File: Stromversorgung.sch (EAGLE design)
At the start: 16 parts, among them J1 DCJ0202, U1 TSR 2-2450, U2 TSR 1-2433, U3 TSR 2-2450, X1 Ein/Aus, X2 MAC64L

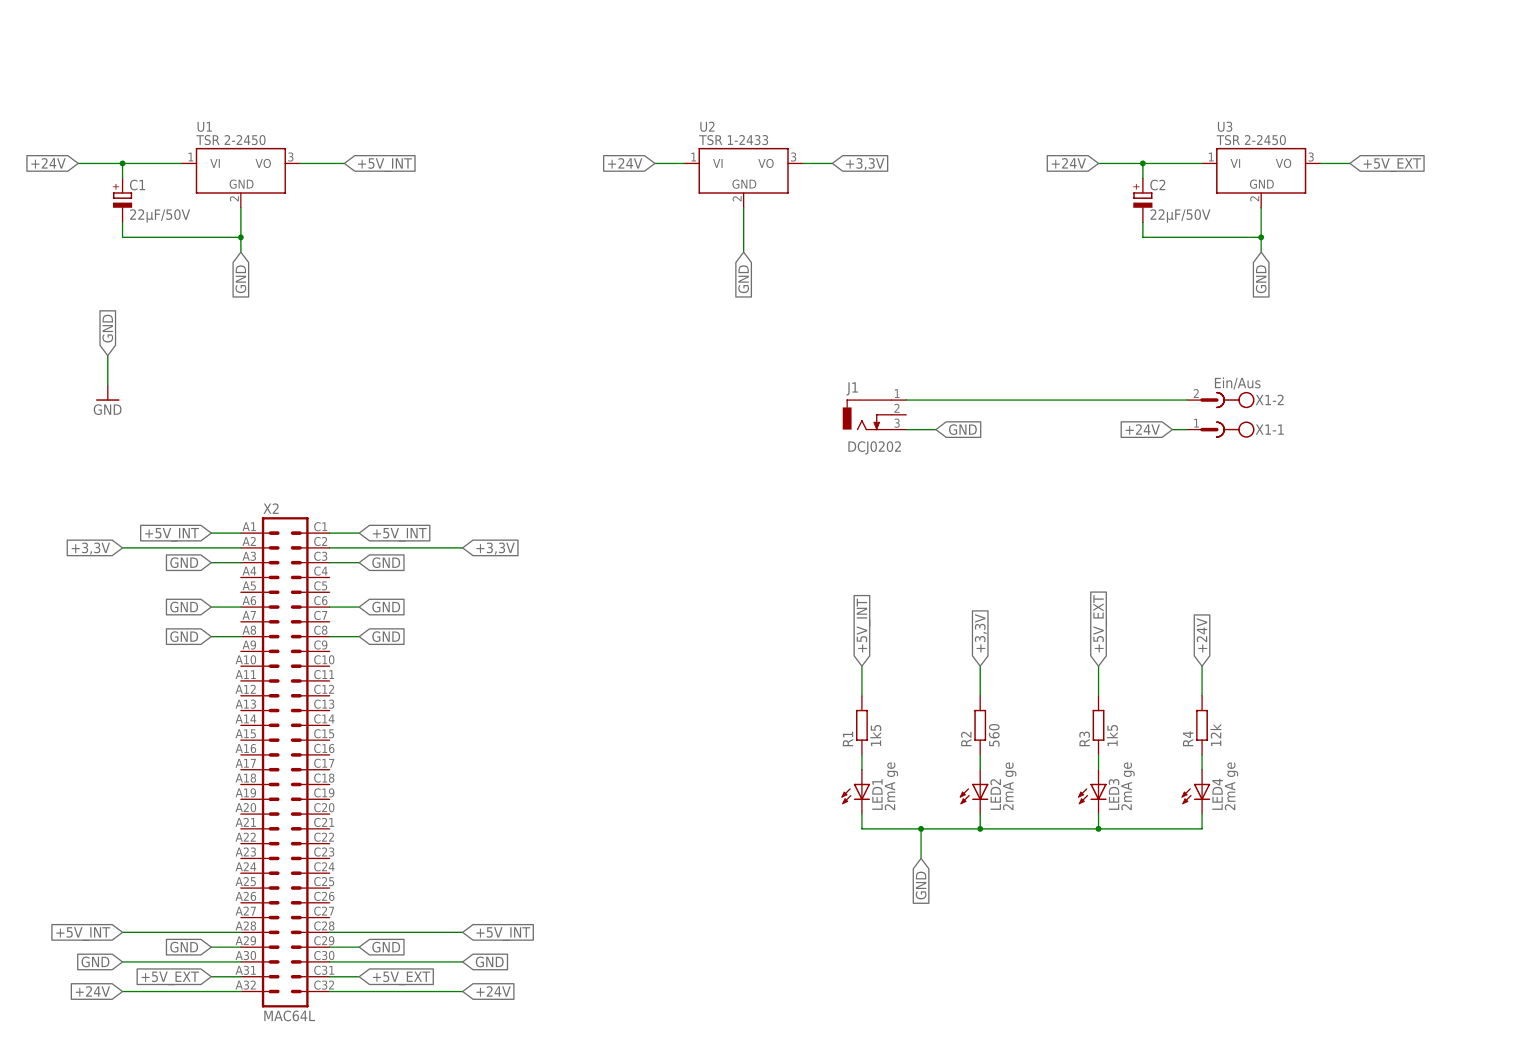
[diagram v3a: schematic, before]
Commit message: 1-Wire Sensor auf Raspi-Platine
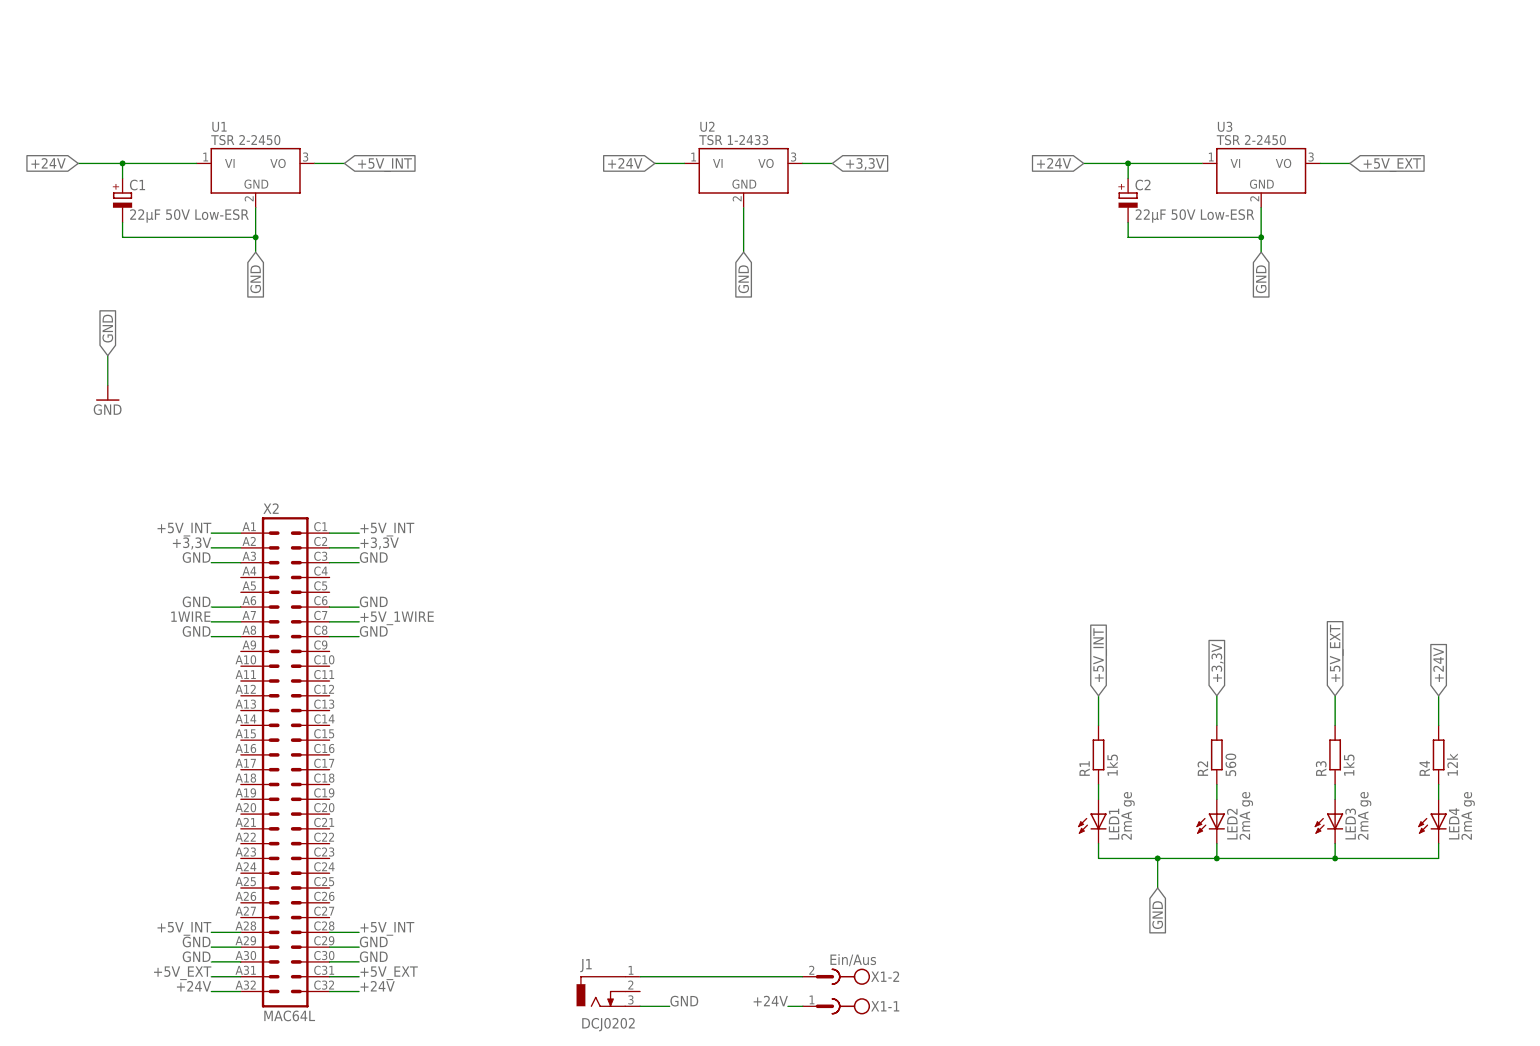
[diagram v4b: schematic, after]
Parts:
- C1, C2: value 22µF/50V -> 22µF 50V Low-ESR
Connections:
- new net +5V_1WIRE: X2.C7
- new net 1WIRE: X2.A7
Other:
- moved on the sheet: C2, J1, LED1, LED2, LED3, LED4, R1, R2, R3, R4, U1, X1-1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

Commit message: Diverse Anpassungen
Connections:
- net +5V_1WIRE renamed !PI_RESET
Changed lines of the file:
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@@
 </segment>
 </net>
-<net name="+5V_1WIRE" class="0">
+<net name="!PI_RESET" class="0">
 <segment>
 <pinref part="X2" gate="G$1" pin="C7"/>
